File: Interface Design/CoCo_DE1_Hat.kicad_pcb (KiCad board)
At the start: 2 copper layers, 103 x 66 mm, 25 parts, among them J1 J1, J2 J2, J3 J3, J4 J4, J5 J5, J6 J6, U1 74LVC245A, U2 74LVC245A, U3 74LVC245A, U4 74LVC245A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

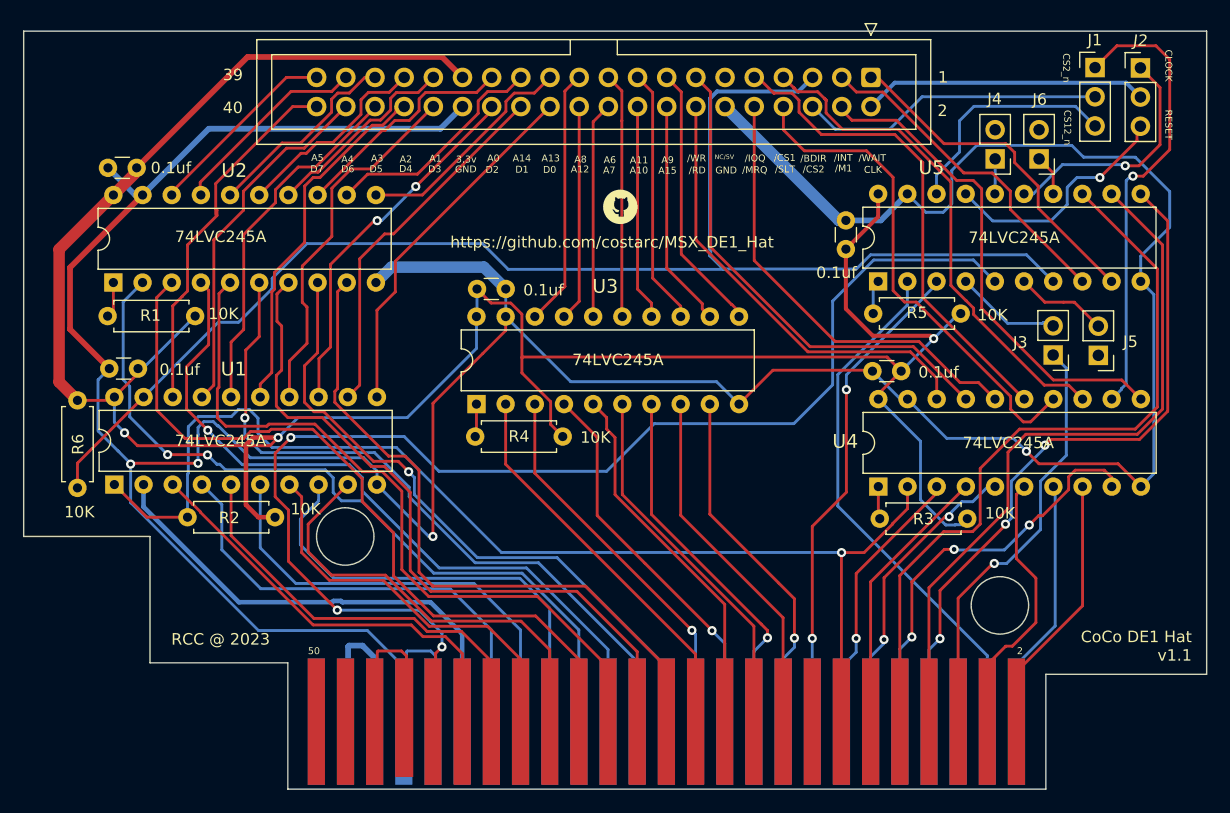
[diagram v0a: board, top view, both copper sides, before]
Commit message: Adding PCB layout
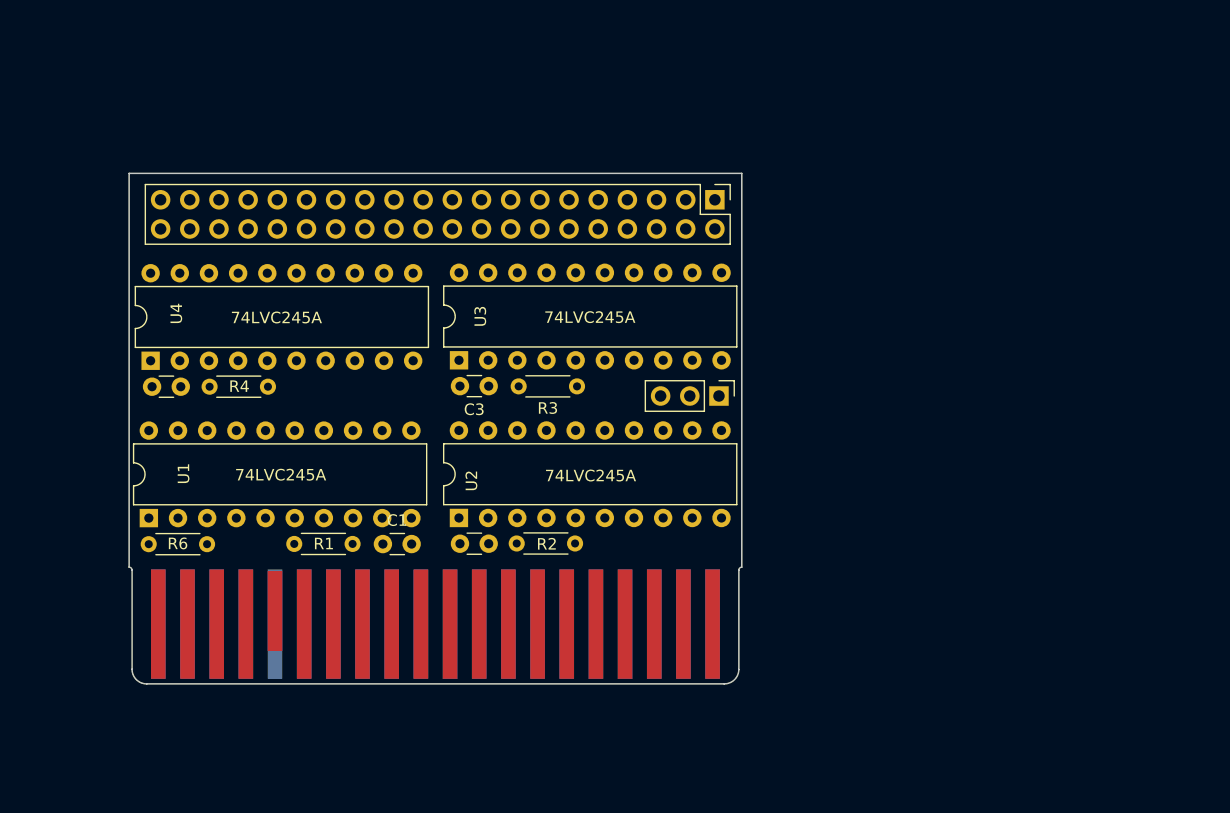
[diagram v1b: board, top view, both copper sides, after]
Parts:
- removed C5: 0.1uf, Capacitor_THT:C_Disc_D3.0mm_W1.6mm_P2.50mm
- removed CONN1: MSX_BUS, Roni Footprints:MSX_CART_SW
- removed G***: LOGO, LOGO
- removed J2: J2, Connector_PinHeader_2.54mm:PinHeader_1x03_P2.54mm_Vertical
- removed J3: J3, Connector_PinHeader_2.54mm:PinHeader_1x02_P2.54mm_Vertical
- removed J4: J4, Connector_PinHeader_2.54mm:PinHeader_1x02_P2.54mm_Vertical
- removed J5: J5, Connector_PinHeader_2.54mm:PinHeader_1x02_P2.54mm_Vertical
- removed J6: J6, Connector_PinHeader_2.54mm:PinHeader_1x02_P2.54mm_Vertical
- removed R5: 10K, Resistor_THT:R_Axial_DIN0207_L6.3mm_D2.5mm_P7.62mm_Horizontal
- removed U5: 74LVC245A, Package_DIP:DIP-20_W7.62mm
- added P1: CoCo_Slot, Roni Footprints:COCO-CART-HAT, F.Cu at (61.1, 77.0)
- IDC1: footprint Connector_IDC:IDC-Header_2x20_P2.54mm_Vertical -> Connector_PinHeader_2.54mm:PinHeader_2x20_P2.54mm_Vertical
- R1, R2, R3, R4, R6: footprint Resistor_THT:R_Axial_DIN0207_L6.3mm_D2.5mm_P7.62mm_Horizontal -> Resistor_THT:R_Axial_DIN0204_L3.6mm_D1.6mm_P5.08mm_Horizontal
- moved U4 64.3 mm to (63.0, 48.9)
- moved C4 62.7 mm to (63.1, 51.2)
- moved C2 46.6 mm to (92.4, 64.8), turned to 180 degrees
- moved J1 43.5 mm to (112.5, 52.0), turned to -90 degrees
- moved U2 36.4 mm to (89.8, 62.6)
- moved R3 35.9 mm to (100.1, 51.1)
- moved C1 28.3 mm to (83.2, 64.9)
- moved R2 26.2 mm to (100.0, 64.8)
- moved R4 26.0 mm to (73.2, 51.2)
- moved R1 21.6 mm to (75.5, 64.8), turned to 0 degrees
- moved IDC1 17.3 mm to (112.1, 34.9)
- moved R6 14.0 mm to (62.8, 64.9), turned to 0 degrees
- moved C3 8.59 mm to (92.4, 51.1)
- moved U1 4.19 mm to (62.8, 62.6)
- moved U3 4.11 mm to (89.8, 48.9)
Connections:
- IDC1 pad 1: /C_WAIT -> unconnected-(IDC1-Pad1)
- IDC1 pad 10: /C_MREQ -> *C_RESET
- IDC1 pad 13: /C_WR -> *C_HALT
- IDC1 pad 14: /C_RD -> *C_NMI
- IDC1 pad 2: C_CLK_OR_RST -> unconnected-(IDC1-Pad2)
- IDC1 pad 3: /C_INT -> unconnected-(IDC1-Pad3)
- IDC1 pad 4: /C_M1 -> unconnected-(IDC1-Pad4)
- IDC1 pad 5: /C_BUSDIR -> *C_SLENB_SCS
- IDC1 pad 6: C_CS2_CS12 -> *C_RW
- IDC1 pad 7: /C_CS1 -> C_E
- IDC1 pad 8: /C_SLTSL -> *C_CTS
- IDC1 pad 9: /C_IORQ -> unconnected-(IDC1-Pad9)
- J1 pad 1: /C_CS2 -> *SLENB
- J1 pad 2: C_CS2_CS12 -> *SLENB_SCS
- J1 pad 3: /C_CS12 -> *SCS
- R1 pad 2: Net-(R1-Pad2) -> *RW
- R2 pad 2: /RD -> Net-(U2-Pad1)
- U1 pad 1: /RD -> *RW
- U1 pad 11: C_D0 -> D0
- U1 pad 12: C_D1 -> D1
- U1 pad 13: C_D2 -> D2
- U1 pad 14: C_D3 -> D3
- U1 pad 15: C_D4 -> D4
- U1 pad 16: C_D5 -> D5
- U1 pad 17: C_D6 -> D6
- U1 pad 18: C_D7 -> D7
- U1 pad 2: D7 -> C_D7
- U1 pad 3: D6 -> C_D6
- U1 pad 4: D5 -> C_D5
- U1 pad 5: D4 -> C_D4
- U1 pad 6: D3 -> C_D3
- U1 pad 7: D2 -> C_D2
- U1 pad 8: D1 -> C_D1
- U1 pad 9: D0 -> C_D0
- U2 pad 1: Net-(R1-Pad2) -> Net-(U2-Pad1)
- U3 pad 1: Net-(R4-Pad2) -> Net-(R3-Pad2)
- U4 pad 1: Net-(R3-Pad2) -> Net-(R4-Pad2)
- U4 pad 11: /C_M1 -> C_E
- U4 pad 12: /C_CS2 -> *HALT
- U4 pad 13: /C_CS1 -> *NMI
- U4 pad 14: /C_SLTSL -> *C_RESET
- U4 pad 15: /C_IORQ -> *C_SLENB_SCS
- U4 pad 16: /C_MREQ -> *C_CTS
- U4 pad 17: /C_WR -> *C_CART
- U4 pad 18: /C_RD -> *C_RW
- U4 pad 2: /RD -> *RW
- U4 pad 3: /WR -> *CART
- U4 pad 4: /MREQ -> *CTS
- U4 pad 5: /IORQ -> *SLENB_SCS
- U4 pad 6: /SLTSL -> *RESET
- U4 pad 7: /CS1 -> *C_NMI
- U4 pad 8: /CS2 -> *C_HALT
- U4 pad 9: /M1 -> E
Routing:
- net GNDREF: track 329.9 -> 0.00 mm, vias 4 -> 0
- net Vdd: track 220.9 -> 0.00 mm, vias 3 -> 0
- net /C_BUSDIR: track 123.0 -> 0.00 mm
- net CLOCK: track 110.9 -> 0.00 mm, vias 3 -> 0
- net /RD: track 102.9 -> 0.00 mm, vias 1 -> 0
- net A5: track 68.1 -> 0.00 mm, vias 2 -> 0
- net A4: track 66.9 -> 0.00 mm
- net /INT: track 66.6 -> 0.00 mm
- net /BUSDIR: track 65.3 -> 0.00 mm
- net A3: track 64.4 -> 0.00 mm, vias 1 -> 0
- net A2: track 64.1 -> 0.00 mm
- net A0: track 61.9 -> 0.00 mm
- net A1: track 61.9 -> 0.00 mm, vias 1 -> 0
- net /WAIT: track 60.1 -> 0.00 mm, vias 3 -> 0
- net A13: track 59.2 -> 0.00 mm
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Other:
- board size 103 x 66 mm -> 53.3 x 44.5 mm
- board text removed: "/BDIR"
- board text removed: "/CS1"
- board text removed: "/CS2"
- board text removed: "/INT"
- board text removed: "/IOQ"
- board text removed: "/M1"
- board text removed: "/MRQ"
- board text removed: "/RD"
- board text removed: "/SLT"
- board text removed: "/WAIT"
- board text removed: "/WR"
- board text removed: "1"
- board text removed: "2"
- board text removed: "3.3v"
- board text removed: "39"
- board text removed: "40"
- board text removed: "49"
- board text removed: "50"
- board text removed: "A0"
- board text removed: "A1"
- board text removed: "A10"
- board text removed: "A11"
- board text removed: "A12"
- board text removed: "A13"
- board text removed: "A14"
- board text removed: "A15"
- board text removed: "A2"
- board text removed: "A3"
- board text removed: "A4"
- board text removed: "A5"
- board text removed: "A6"
- board text removed: "A7"
- board text removed: "A8"
- board text removed: "A9"
- board text removed: "CLK"
- board text removed: "CLOCK"
- board text removed: "CS12_n"
- board text removed: "CS2_n"
- board text removed: "CoCo DE1 Hat v1.1"
- board text removed: "D0"
- board text removed: "D1"
- board text removed: "D2"
- board text removed: "D3"
- board text removed: "D4"
- board text removed: "D5"
- board text removed: "D6"
- board text removed: "D7"
- board text removed: "GND"
- board text removed: "NC/5V"
- board text removed: "RCC @ 2023"
- board text removed: "RESET"
- board text removed: "https://github.com/costarc/MSX_DE1_Hat"

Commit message: Project completd
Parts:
- added G***: LOGO, LOGO, F.Cu at (102.7, 51.9)
- added G***: LOGO, LOGO, B.Cu at (87.4, 45.8)
- moved J1 31.4 mm to (81.1, 52.0)
- moved C4 2.32 mm to (65.4, 51.2), turned to 180 degrees
- moved C2 0.15 mm to (92.4, 65.0)
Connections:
- IDC1 pad 1: unconnected-(IDC1-Pad1) -> C_A14
- IDC1 pad 10: *C_RESET -> C_A5
- IDC1 pad 13: *C_HALT -> unconnected-(IDC1-Pad13)
- IDC1 pad 14: *C_NMI -> unconnected-(IDC1-Pad14)
- IDC1 pad 15: C_A9 -> /C_BUSDIR
- IDC1 pad 16: C_A15 -> unconnected-(IDC1-Pad16)
- IDC1 pad 17: C_A11 -> C_A10
- IDC1 pad 18: C_A10 -> C_A12
- IDC1 pad 2: unconnected-(IDC1-Pad2) -> C_A15
- IDC1 pad 20: C_A7 -> C_A8
- IDC1 pad 21: C_A8 -> C_A0
- IDC1 pad 22: C_A12 -> C_A4
- IDC1 pad 23: C_A13 -> C_A1
- IDC1 pad 24: C_D0 -> C_A2
- IDC1 pad 25: C_A14 -> C_Q
- IDC1 pad 26: C_D1 -> C_D7
- IDC1 pad 27: C_A0 -> C_D5
- IDC1 pad 28: C_D2 -> C_D6
- IDC1 pad 3: unconnected-(IDC1-Pad3) -> *C_SCS
- IDC1 pad 31: C_A1 -> *C_HALT
- IDC1 pad 32: C_D3 -> *C_CART
- IDC1 pad 33: C_A2 -> C_D4
- IDC1 pad 34: C_D4 -> *C_RW
- IDC1 pad 35: C_A3 -> C_D3
- IDC1 pad 36: C_D5 -> *C_RESET
- IDC1 pad 37: C_A4 -> C_D2
- IDC1 pad 38: C_D6 -> *C_NMI_SLENB
- IDC1 pad 39: C_A5 -> C_D1
- IDC1 pad 4: unconnected-(IDC1-Pad4) -> C_A13
- IDC1 pad 40: C_D7 -> C_D0
- IDC1 pad 5: *C_SLENB_SCS -> *C_CTS
- IDC1 pad 6: *C_RW -> C_A11
- IDC1 pad 7: C_E -> C_A9
- IDC1 pad 8: *C_CTS -> C_A7
- IDC1 pad 9: unconnected-(IDC1-Pad9) -> C_A3
- J1 pad 2: *SLENB_SCS -> *NMI_SLENB
- J1 pad 3: *SCS -> *NMI
- P1 pad 18: *RW -> Net-(P1-Pad18)
- P1 pad 35: SND -> unconnected-(P1-Pad35)
- P1 pad 6: E -> unconnected-(P1-Pad6)
- R1 pad 2: *RW -> Net-(P1-Pad18)
- U1 pad 1: *RW -> Net-(P1-Pad18)
- U1 pad 11: D0 -> D7
- U1 pad 12: D1 -> D6
- U1 pad 13: D2 -> D5
- U1 pad 14: D3 -> D4
- U1 pad 15: D4 -> D3
- U1 pad 16: D5 -> D2
- U1 pad 17: D6 -> D1
- U1 pad 18: D7 -> D0
- U1 pad 2: C_D7 -> C_D0
- U1 pad 3: C_D6 -> C_D1
- U1 pad 4: C_D5 -> C_D2
- U1 pad 5: C_D4 -> C_D3
- U1 pad 6: C_D3 -> C_D4
- U1 pad 7: C_D2 -> C_D5
- U1 pad 8: C_D1 -> C_D6
- U1 pad 9: C_D0 -> C_D7
- U2 pad 11: C_A13 -> C_A15
- U2 pad 12: C_A14 -> C_A13
- U2 pad 13: C_A0 -> C_A12
- U2 pad 14: C_A1 -> C_A10
- U2 pad 15: C_A2 -> C_A8
- U2 pad 16: C_A3 -> C_A6
- U2 pad 18: C_A5 -> C_A2
- U2 pad 2: A5 -> A2
- U2 pad 4: A3 -> A6
- U2 pad 5: A2 -> A8
- U2 pad 6: A1 -> A10
- U2 pad 7: A0 -> A12
- U2 pad 8: A14 -> A13
- U2 pad 9: A13 -> A15
- U3 pad 11: C_A9 -> C_A14
- U3 pad 12: C_A15 -> *C_SCS
- U3 pad 13: C_A11 -> *C_CTS
- U3 pad 14: C_A10 -> C_A11
- U3 pad 15: C_A6 -> C_A9
- U3 pad 17: C_A12 -> C_A5
- U3 pad 18: C_A8 -> C_A3
- U3 pad 2: A8 -> A3
- U3 pad 3: A12 -> A5
- U3 pad 5: A6 -> A9
- U3 pad 6: A10 -> A11
- U3 pad 7: A11 -> *CTS
- U3 pad 8: A15 -> *SCS
- U3 pad 9: A9 -> A14
- U4 pad 11: C_E -> C_A0
- U4 pad 12: *HALT -> C_A1
- U4 pad 13: *NMI -> C_Q
- U4 pad 14: *C_RESET -> *CART
- U4 pad 15: *C_SLENB_SCS -> *HALT
- U4 pad 16: *C_CTS -> *C_RW
- U4 pad 17: *C_CART -> *C_RESET
- U4 pad 18: *C_RW -> *NMI_SLENB
- U4 pad 2: *RW -> *C_NMI_SLENB
- U4 pad 3: *CART -> *RESET
- U4 pad 4: *CTS -> *RW
- U4 pad 5: *SLENB_SCS -> *C_HALT
- U4 pad 6: *RESET -> *C_CART
- U4 pad 7: *C_NMI -> Q
- U4 pad 8: *C_HALT -> A1
- U4 pad 9: E -> A0
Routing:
- net GNDREF: track 0.00 -> 212.7 mm, vias 0 -> 5
- net Vdd: track 0.00 -> 165.0 mm, vias 0 -> 3
- net /C_BUSDIR: track 0.00 -> 68.7 mm, vias 0 -> 1
- net *SLENB: track 0.00 -> 49.2 mm
- net *NMI: track 0.00 -> 45.7 mm
- net *CART: track 0.00 -> 43.7 mm, vias 0 -> 2
- net *HALT: track 0.00 -> 42.3 mm, vias 0 -> 3
- net *NMI_SLENB: track 0.00 -> 33.3 mm
- net C_D2: track 0.00 -> 30.2 mm
- net C_A12: track 0.00 -> 29.7 mm
- net C_D5: track 0.00 -> 29.6 mm
- net Net-(P1-Pad18): track 0.00 -> 29.6 mm
- net C_D1: track 0.00 -> 29.5 mm
- net C_D3: track 0.00 -> 29.4 mm
- net C_D4: track 0.00 -> 29.4 mm
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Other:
- board text added: "*CTS A11"
- board text added: "*HALT *CART"
- board text added: "*NMI"
- board text added: "*SCS A13"
- board text added: "*SLENB"
- board text added: "1"
- board text added: "2"
- board text added: "39"
- board text added: "3V GND"
- board text added: "40"
- board text added: "5V GND"
- board text added: "A0 A4"
- board text added: "A1 A2"
- board text added: "A10 A12"
- board text added: "A14 A15"
- board text added: "A3 A5"
- board text added: "A6 A8"
- board text added: "A9 A7"
- board text added: "CP 400 Color"
- board text added: "CoCo DE1 Hat Rev 0"
- board text added: "Compatible"
- board text added: "D1 D0"
- board text added: "D2 P38"
- board text added: "D3 *RST"
- board text added: "D4 *RW"
- board text added: "D5 D6"
- board text added: "NC NC"
- board text added: "Q D7"
- board text added: "RCC@2023"
- board text added: "https://github.com/costarc/CoCo_DE1_Hat"

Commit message: Small change to silk
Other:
- board text added: "P38"
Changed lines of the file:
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@@
+    (effects (font (size 0.5 0.5) (thickness 0.125)))
+  )
+  (gr_text "P38" (at 78.62 53.72) (layer "F.SilkS")
     (effects (font (size 0.5 0.5) (thickness 0.125)))
   )
